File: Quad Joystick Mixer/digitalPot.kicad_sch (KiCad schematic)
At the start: 13 parts, among them U4 OPA1692xD

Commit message: work through digital pot circuit
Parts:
- added C13 (x5): 0.1uF, Capacitor_SMD:C_0805_2012Metric_Pad1.18x1.45mm_HandSolder, symbol Device:C
- added R25, R26, R27: 10k, symbol Device:R_US
- added U4: OPA1692xD, Package_SO:SOIC-8_3.9x4.9mm_P1.27mm, symbol Amplifier_Operational:OPA1692xD
- added U9: ~, Package_SO:SOIC-16_3.9x9.9mm_P1.27mm, symbol Eyewool ICs:DS1881Z-050+
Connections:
- net +12V: now also C13.1, U4.8 (V+)
- net -12V: now also C13.1, U4.4 (V-)
- net GND: now also C13.2, C13.2, C13.2, U9.1 (GND)
- net Mix_Input: now also U9.10 (H1), U9.8 (H0)
- net VCC: now also C13.1, U9.15 (VCC)
- net at U8.12 (nCE): now also R25.1
- net SDA: now reaches U8.13 (SDA)
- net SDA: now also U9.13 (SDA)
- net SCL: now reaches U8.14 (SCL)
- net SCL: now also U9.14 (SCL)
- net +3.3V: now reaches U8.16 (VDD)
- net +3.3V: now also C13.1, C13.1, R27.1, U9.16 (VDD)
- net Earth: now reaches U8.2 (A2)
- net Earth: now also U8.3 (A1), U8.5 (A0), C13.2, C13.2, R25.2, R26.2, U9.2 (A2), U9.3 (A1)
- net at U4.1, U4.2 (-), U8.7 (L0)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: now also U9.7 (L0), U9.9 (L1)
- net at R23.1, R8.2, U4.3 (+): now also U4.5 (+)
- net OUTB: now reaches U4.6 (-), U4.7
- net at U4.6 (-): now also U4.7
- net OUTA: now reaches U4.1, U4.2 (-)
- new net: R26.1, U9.12 (nCE)
- new net: R27.2, U9.5 (A0)
- new net: U4.3 (+), U9.6 (W0)
- new net: U4.5 (+), U9.11 (W1)
- new net OUTC: U4.1, U4.2 (-)
- new net OUTD: U4.6 (-), U4.7
- no-connect marks 1 -> 2
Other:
- moved on the sheet: C13, C2, R14, R23, R8, U4A, U4B, U4C, U8

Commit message: working on finishing a draft of this dang schematic
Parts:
- added C2 (x4): 1uF, Capacitor_SMD:C_0805_2012Metric_Pad1.18x1.45mm_HandSolder, symbol Device:C
- added D16: BZT52C4V7-13-F, symbol Device:D_Zener
- added R14 (x4): 100k, symbol Device:R_US
- added R34 (x4): 1k, symbol Device:R_US
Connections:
- net GND: now also D16.2 (A), R14.2, R14.2, R14.2, R14.2
- net Mix_Input: now also D16.1 (K)
- net OUTA: now also R34.1; no longer U4.1, U4.2 (-)
- net OUTB: now also R34.1; no longer U4.6 (-), U4.7
- net OUTC: now also R34.1; no longer U4.1, U4.2 (-)
- net OUTD: now also R34.1; no longer U4.6 (-), U4.7
- new net: C2.1, U4.6 (-), U4.7 (x2)
- new net: C2.1, U4.1, U4.2 (-) (x2)
- new net: C2.2, R14.1, R34.2 (x4)
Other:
- moved on the sheet: C2, R14

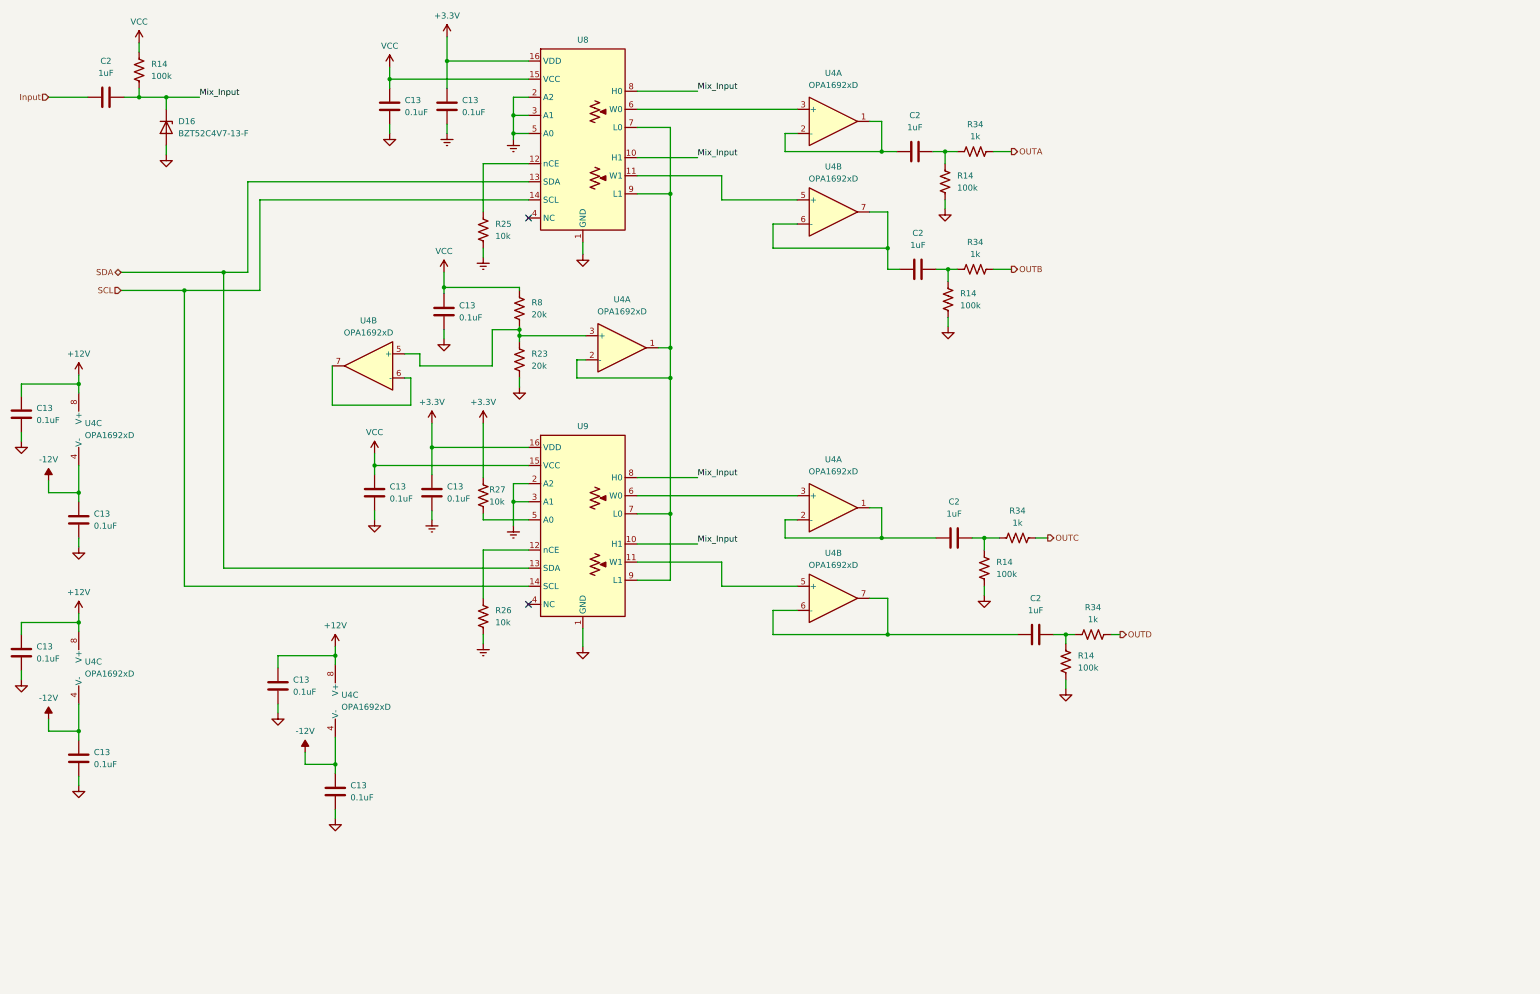
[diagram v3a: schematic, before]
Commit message: add in rotary circuit and some docs
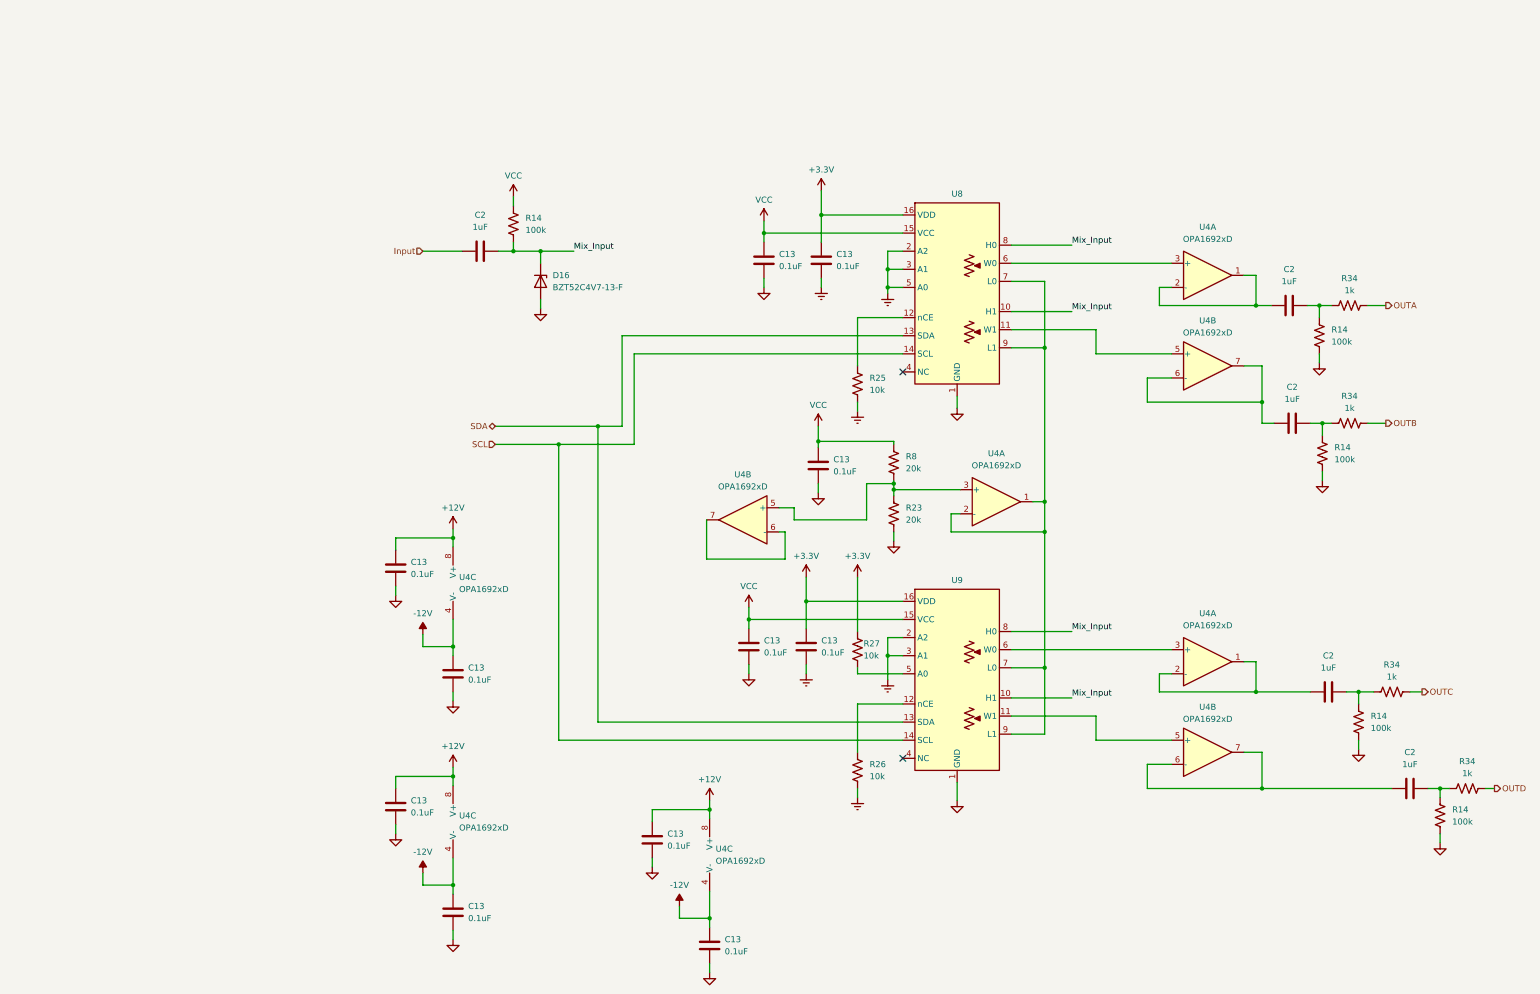
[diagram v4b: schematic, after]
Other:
- moved on the sheet: C13, C2, D16, R14, R23, R25, R26, R27, R34, R8, U4A, U4B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

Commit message: finished first draft of the schematic
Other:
- note added: "Digital Pots"
- title: (none) -> Quadrophonic Joystick Mixer
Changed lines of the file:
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@@
   (paper "B")
   (title_block
+    (title "Quadrophonic Joystick Mixer")
     (date "2024-02-14")
+    (rev "P1")
   )
   (junction (at 206.375 151.13) (diameter 0) (color 0 0 0 0)
@@
     (stroke (width 0) (type default))
   )
+  (text "Digital Pots" (at 169.545 32.385 0)
+    (effects (font (size 3.81 3.81) (thickness 0.508) bold) (justify left bottom))
+  )
   (label "Mix_Input" (at 245.11 78.74 0) (fields_autoplaced)

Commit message: ok the draft wasn't done but now i think it is
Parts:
- added TP1 (x4): TestPoint, TestPoint:TestPoint_THTPad_D1.5mm_Drill0.7mm, symbol Connector:TestPoint
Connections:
- net at U4.5 (+), U8.11 (W1): now also TP1.1
- net at U4.3 (+), U8.6 (W0): now also TP1.1
- net at U4.3 (+), U9.6 (W0): now also TP1.1
- net at U4.5 (+), U9.11 (W1): now also TP1.1
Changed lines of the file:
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@@
   (junction (at 206.375 151.13) (diameter 0) (color 0 0 0 0)
   )
+  (junction (at 255.27 68.58) (diameter 0) (color 0 0 0 0)
+  )
   (junction (at 137.16 106.68) (diameter 0) (color 0 0 0 0)
   )
@@
   (junction (at 189.23 139.7) (diameter 0) (color 0 0 0 0)
   )
+  (junction (at 254.635 87.63) (diameter 0) (color 0 0 0 0)
+  )
   (junction (at 191.77 106.045) (diameter 0) (color 0 0 0 0)
   )
@@
   (junction (at 305.435 158.75) (diameter 0) (color 0 0 0 0)
   )
+  (junction (at 254.635 149.86) (diameter 0) (color 0 0 0 0)
+  )
+  (junction (at 254.635 168.91) (diameter 0) (color 0 0 0 0)
+  )
   (junction (at 207.645 114.935) (diameter 0) (color 0 0 0 0)
   )
@@
     (stroke (width 0) (type default))
   )
+  (wire (pts (xy 255.27 68.58) (xy 266.065 68.58))
+    (stroke (width 0) (type default))
+  )
   (wire (pts (xy 200.025 80.01) (xy 200.025 90.17))
     (stroke (width 0) (type default))
@@
     (stroke (width 0) (type default))
   )
+  (wire (pts (xy 255.27 66.04) (xy 255.27 68.58))
+    (stroke (width 0) (type default))
+  )
   (wire (pts (xy 283.845 158.75) (xy 295.275 158.75))
     (stroke (width 0) (type default))
@@
     (stroke (width 0) (type default))
   )
+  (wire (pts (xy 255.905 84.455) (xy 254.635 84.455))
+    (stroke (width 0) (type default))
+  )
   (wire (pts (xy 114.935 149.225) (xy 114.935 151.13))
     (stroke (width 0) (type default))
@@
     (stroke (width 0) (type default))
   )
+  (wire (pts (xy 255.905 166.37) (xy 254.635 166.37))
+    (stroke (width 0) (type default))
+  )
   (wire (pts (xy 297.815 102.235) (xy 297.815 104.775))
     (stroke (width 0) (type default))
@@
     (stroke (width 0) (type default))
   )
-  (wire (pts (xy 250.19 87.63) (xy 266.065 87.63))
+  (wire (pts (xy 250.19 87.63) (xy 254.635 87.63))
+    (stroke (width 0) (type default))
+  )
+  (wire (pts (xy 254.635 166.37) (xy 254.635 168.91))
     (stroke (width 0) (type default))
   )
@@
     (stroke (width 0) (type default))
   )
+  (wire (pts (xy 254.635 146.685) (xy 254.635 149.86))
+    (stroke (width 0) (type default))
+  )
   (wire (pts (xy 297.18 77.47) (xy 299.72 77.47))
     (stroke (width 0) (type default))
@@
     (stroke (width 0) (type default))
   )
+  (wire (pts (xy 254.635 149.86) (xy 266.065 149.86))
+    (stroke (width 0) (type default))
+  )
   (wire (pts (xy 114.935 158.75) (xy 114.935 160.655))
     (stroke (width 0) (type default))
@@
     (stroke (width 0) (type default))
   )
-  (wire (pts (xy 232.41 149.86) (xy 266.065 149.86))
+  (wire (pts (xy 232.41 149.86) (xy 254.635 149.86))
     (stroke (width 0) (type default))
   )
@@
     (stroke (width 0) (type default))
   )
-  (wire (pts (xy 232.41 68.58) (xy 266.065 68.58))
+  (wire (pts (xy 232.41 68.58) (xy 255.27 68.58))
     (stroke (width 0) (type default))
   )
@@
     (stroke (width 0) (type default))
   )
+  (wire (pts (xy 256.54 66.04) (xy 255.27 66.04))
+    (stroke (width 0) (type default))
+  )
   (wire (pts (xy 316.23 158.75) (xy 318.77 158.75))
     (stroke (width 0) (type default))
   )
-  (wire (pts (xy 250.19 168.91) (xy 266.065 168.91))
+  (wire (pts (xy 250.19 168.91) (xy 254.635 168.91))
     (stroke (width 0) (type default))
   )
@@
     (stroke (width 0) (type default))
   )
+  (wire (pts (xy 254.635 87.63) (xy 266.065 87.63))
+    (stroke (width 0) (type default))
+  )
   (wire (pts (xy 232.41 153.67) (xy 239.395 153.67))
     (stroke (width 0) (type default))
@@
     (stroke (width 0) (type default))
   )
+  (wire (pts (xy 255.905 146.685) (xy 254.635 146.685))
+    (stroke (width 0) (type default))
+  )
   (wire (pts (xy 263.525 154.94) (xy 266.065 154.94))
     (stroke (width 0) (type default))
@@
     (stroke (width 0) (type default))
   )
+  (wire (pts (xy 254.635 168.91) (xy 266.065 168.91))
+    (stroke (width 0) (type default))
+  )
   (wire (pts (xy 302.895 158.75) (xy 305.435 158.75))
     (stroke (width 0) (type default))
@@
     (stroke (width 0) (type default))
   )
+  (wire (pts (xy 254.635 84.455) (xy 254.635 87.63))
+    (stroke (width 0) (type default))
+  )
   (wire (pts (xy 137.16 168.91) (xy 137.16 106.68))
     (stroke (width 0) (type default))
@@
     )
   )
+  (symbol (lib_id "Connector:TestPoint") (at 255.905 146.685 270) (unit 1)
+    (in_bom yes) (on_board yes) (dnp no) (fields_autoplaced)
+    (property "Reference" "TP1" (at 261.62 146.685 90)
+      (effects (font (size 1.27 1.27)) (justify left))
+    )
+    (property "Value" "TestPoint" (at 257.937 148.59 0)
+      (effects (font (size 1.27 1.27)) (justify left) hide)
+    )
+    (property "Footprint" "TestPoint:TestPoint_THTPad_D1.5mm_Drill0.7mm" (at 255.905 151.765 0)
+      (effects (font (size 1.27 1.27)) hide)
+    )
+    (property "Datasheet" "~" (at 255.905 151.765 0)
+      (effects (font (size 1.27 1.27)) hide)
+    )
+    (pin "1")
+    (instances
+      (project "Quad Joystick Mixer"
+        (path "/e9da4955-68c1-4335-ab8e-8a9cc0328d2d/70e873e8-c2f7-42de-91d7-3f147d0d972e"
+          (reference "TP1") (unit 1)
+        )
+        (path "/e9da4955-68c1-4335-ab8e-8a9cc0328d2d/2ccd8f18-0cde-4a72-a705-f74f6a422b9f"
+          (reference "TP12") (unit 1)
+        )
+        (path "/e9da4955-68c1-4335-ab8e-8a9cc0328d2d/6b806f6d-da33-48ec-b81c-6968195ad9ad"
+          (reference "TP13") (unit 1)
+        )
+      )
+    )
+  )
   (symbol (lib_id "Device:C") (at 114.935 154.94 0) (unit 1)
     (in_bom yes) (on_board yes) (dnp no) (fields_autoplaced)
@@
     )
   )
+  (symbol (lib_id "Connector:TestPoint") (at 256.54 66.04 270) (unit 1)
+    (in_bom yes) (on_board yes) (dnp no) (fields_autoplaced)
+    (property "Reference" "TP1" (at 262.255 66.04 90)
+      (effects (font (size 1.27 1.27)) (justify left))
+    )
+    (property "Value" "TestPoint" (at 258.572 67.945 0)
+      (effects (font (size 1.27 1.27)) (justify left) hide)
+    )
+    (property "Footprint" "TestPoint:TestPoint_THTPad_D1.5mm_Drill0.7mm" (at 256.54 71.12 0)
+      (effects (font (size 1.27 1.27)) hide)
+    )
+    (property "Datasheet" "~" (at 256.54 71.12 0)
+      (effects (font (size 1.27 1.27)) hide)
+    )
+    (pin "1")
+    (instances
+      (project "Quad Joystick Mixer"
+        (path "/e9da4955-68c1-4335-ab8e-8a9cc0328d2d/70e873e8-c2f7-42de-91d7-3f147d0d972e"
+          (reference "TP1") (unit 1)
+        )
+        (path "/e9da4955-68c1-4335-ab8e-8a9cc0328d2d/2ccd8f18-0cde-4a72-a705-f74f6a422b9f"
+          (reference "TP8") (unit 1)
+        )
+        (path "/e9da4955-68c1-4335-ab8e-8a9cc0328d2d/6b806f6d-da33-48ec-b81c-6968195ad9ad"
+          (reference "TP9") (unit 1)
+        )
+      )
+    )
+  )
   (symbol (lib_id "power:VCC") (at 127.635 54.61 0) (unit 1)
     (in_bom yes) (on_board yes) (dnp no) (fields_autoplaced)
@@
     )
   )
+  (symbol (lib_id "Connector:TestPoint") (at 255.905 84.455 270) (unit 1)
+    (in_bom yes) (on_board yes) (dnp no) (fields_autoplaced)
+    (property "Reference" "TP1" (at 261.62 84.455 90)
+      (effects (font (size 1.27 1.27)) (justify left))
+    )
+    (property "Value" "TestPoint" (at 257.937 86.36 0)
+      (effects (font (size 1.27 1.27)) (justify left) hide)
+    )
+    (property "Footprint" "TestPoint:TestPoint_THTPad_D1.5mm_Drill0.7mm" (at 255.905 89.535 0)
+      (effects (font (size 1.27 1.27)) hide)
+    )
+    (property "Datasheet" "~" (at 255.905 89.535 0)
+      (effects (font (size 1.27 1.27)) hide)
+    )
+    (pin "1")
+    (instances
+      (project "Quad Joystick Mixer"
+        (path "/e9da4955-68c1-4335-ab8e-8a9cc0328d2d/70e873e8-c2f7-42de-91d7-3f147d0d972e"
+          (reference "TP1") (unit 1)
+        )
+        (path "/e9da4955-68c1-4335-ab8e-8a9cc0328d2d/2ccd8f18-0cde-4a72-a705-f74f6a422b9f"
+          (reference "TP10") (unit 1)
+        )
+        (path "/e9da4955-68c1-4335-ab8e-8a9cc0328d2d/6b806f6d-da33-48ec-b81c-6968195ad9ad"
+          (reference "TP11") (unit 1)
+        )
+      )
+    )
+  )
   (symbol (lib_id "Amplifier_Operational:OPA1692xD") (at 168.91 193.04 0) (unit 3)
     (in_bom yes) (on_board yes) (dnp no) (fields_autoplaced)
@@
         )
       )
+    )
+  )
+  (symbol (lib_id "Connector:TestPoint") (at 255.905 166.37 270) (unit 1)
+    (in_bom yes) (on_board yes) (dnp no) (fields_autoplaced)
+    (property "Reference" "TP1" (at 261.62 166.37 90)
+      (effects (font (size 1.27 1.27)) (justify left))
+    )
+    (property "Value" "TestPoint" (at 257.937 168.275 0)
+      (effects (font (size 1.27 1.27)) (justify left) hide)
+    )
+    (property "Footprint" "TestPoint:TestPoint_THTPad_D1.5mm_Drill0.7mm" (at 255.905 171.45 0)
+      (effects (font (size 1.27 1.27)) hide)
+    )
+    (property "Datasheet" "~" (at 255.905 171.45 0)
+      (effects (font (size 1.27 1.27)) hide)
+    )
+    (pin "1")
+    (instances
+      (project "Quad Joystick Mixer"
+        (path "/e9da4955-68c1-4335-ab8e-8a9cc0328d2d/70e873e8-c2f7-42de-91d7-3f147d0d972e"
+          (reference "TP1") (unit 1)
+        )
+        (path "/e9da4955-68c1-4335-ab8e-8a9cc0328d2d/2ccd8f18-0cde-4a72-a705-f74f6a422b9f"
+          (reference "TP14") (unit 1)
+        )
+        (path "/e9da4955-68c1-4335-ab8e-8a9cc0328d2d/6b806f6d-da33-48ec-b81c-6968195ad9ad"
+          (reference "TP15") (unit 1)
+        )
+      )

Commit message: clean up after review, working through BOM
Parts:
- D16: footprint (none) -> BZT52C4V7-13-F; DK PN (none) -> BZT52C4V7-13FDICT-ND; MPN (none) -> BZT52C4V7-13-F
- R34: value 1k -> 10k
- U8, U9: value ~ -> DS1881Z-050+; DK PN (none) -> DS1881Z-050+-ND; MPN (none) -> DS1881Z-050+
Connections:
- net VCC: no longer R14.1
- net VDD: now reaches U4.1, U4.2 (-), U8.7 (L0), U8.9 (L1), U9.7 (L0), U9.9 (L1)
- net VDD: now also R14.1, U4.6 (-), U4.7
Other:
- note added: "VDD is mid-supply for bias"
- moved on the sheet: U4B

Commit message: finish adding parts to the BOM
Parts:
- C13, C2, D16, U8, U9: Source (none) -> DK
- R14: footprint (none) -> Resistor_SMD:R_0805_2012Metric_Pad1.20x1.40mm_HandSolder; DK PN (none) -> RMCF0805FT100KCT-ND; MPN (none) -> RMCF0805FT100K; Source (none) -> DK
- R23, R8: footprint (none) -> Resistor_SMD:R_0805_2012Metric_Pad1.20x1.40mm_HandSolder; DK PN (none) -> RMCF0805FT20K0CT-ND; MPN (none) -> RMCF0805FT20K0; Source (none) -> DK
- R25, R26, R27, R34: footprint (none) -> Resistor_SMD:R_0805_2012Metric_Pad1.20x1.40mm_HandSolder; DK PN (none) -> RMCF0805JT10K0CT-ND; MPN (none) -> RMCF0805JT10K0; Source (none) -> DK
- TP1: Source (none) -> NA
- U4: value OPA1692xD -> TL072; DK PN (none) -> 296-TL072HIDRCT-ND; MPN (none) -> TL072HIDR; Source (none) -> DK
